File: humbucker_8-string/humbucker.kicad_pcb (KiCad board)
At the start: 2 copper layers, 102 parts, among them J1 CONN_02X04, J2 CONN_01X03, U1/2 TL072, U3/4 TL072, U5/6 TL072, U7/8 TL072

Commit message: humbucker fix
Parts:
- turned C11 to 0 degrees
- turned C31 to 0 degrees
- turned C32 to 0 degrees
- turned C51 to 0 degrees
- turned C71 to 0 degrees
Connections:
- C11 pad 1: Net-(C11-Pad1) -> GND
- C12 pad 1: +9V -> GND
- C12 pad 2: Net-(C12-Pad2) -> +9V
- C31 pad 1: Net-(C31-Pad1) -> GND
- C32 pad 2: Net-(C32-Pad2) -> GND
- C51 pad 1: Net-(C51-Pad1) -> GND
- C52 pad 1: +9V -> GND
- C52 pad 2: Net-(C52-Pad2) -> +9V
- C71 pad 1: Net-(C71-Pad1) -> GND
- C72 pad 1: +9V -> GND
- C72 pad 2: Net-(C72-Pad2) -> +9V
- U1/2 pad 4: Net-(C11-Pad1) -> -9VA
- U1/2 pad 8: Net-(C12-Pad2) -> +9V
- U3/4 pad 4: Net-(C31-Pad1) -> -9VA
- U3/4 pad 8: Net-(C32-Pad2) -> +9V
- U5/6 pad 4: Net-(C51-Pad1) -> -9VA
- U5/6 pad 8: Net-(C52-Pad2) -> +9V
- U7/8 pad 4: Net-(C71-Pad1) -> -9VA
- U7/8 pad 8: Net-(C72-Pad2) -> +9V
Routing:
- net GND: track 309.6 -> 363.5 mm, vias 0 -> 8
- net -9VA: track 130.8 -> 153.2 mm
- net +9V: track 102.6 -> 122.1 mm
- net Net-(C72-Pad2): track 2.55 -> 0.00 mm
- net Net-(C52-Pad2): track 2.55 -> 0.00 mm
- net Net-(C51-Pad1): track 2.55 -> 0.00 mm
- net Net-(C31-Pad1): track 2.55 -> 0.00 mm
- net Net-(C12-Pad2): track 2.55 -> 0.00 mm
- net Net-(C11-Pad1): track 2.55 -> 0.00 mm
- net Net-(C71-Pad1): track 2.44 -> 0.00 mm
- net Net-(C32-Pad2): track 2.44 -> 0.00 mm

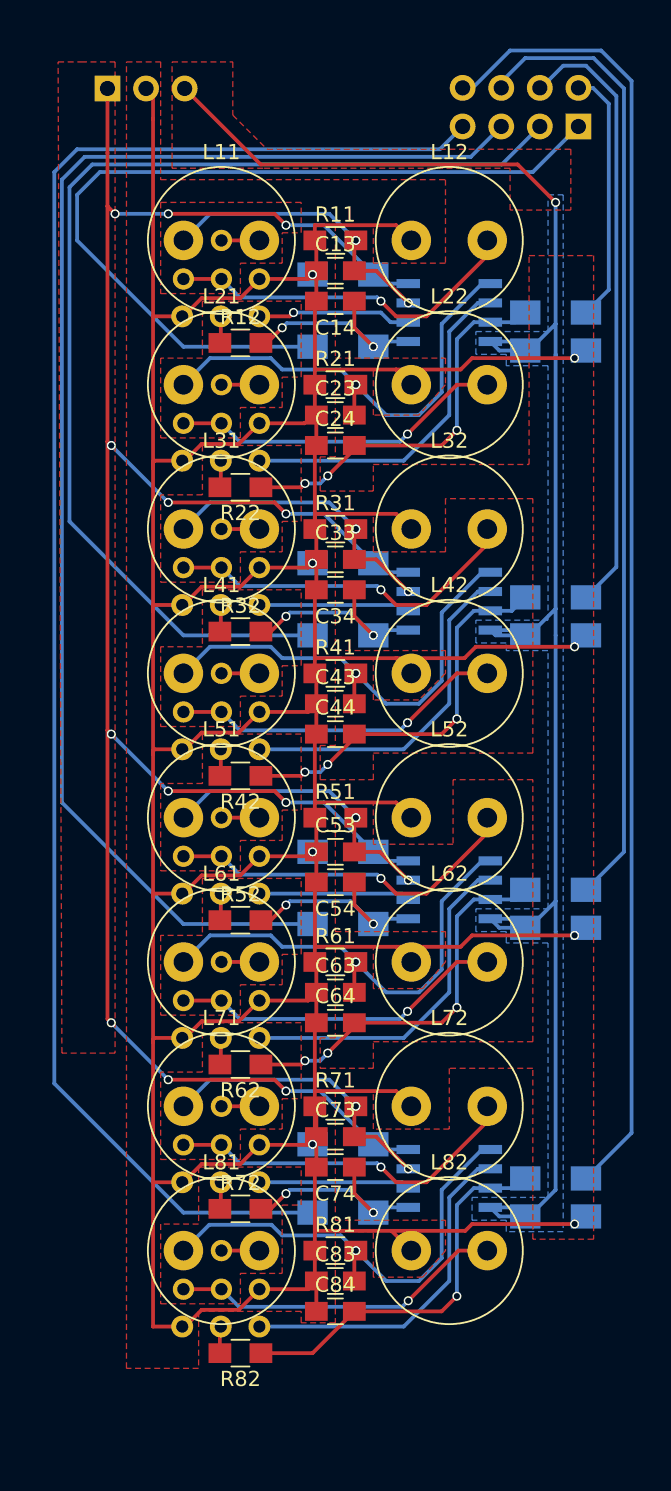
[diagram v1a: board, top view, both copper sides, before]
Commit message: humbucker: add mounting holes & dimensions
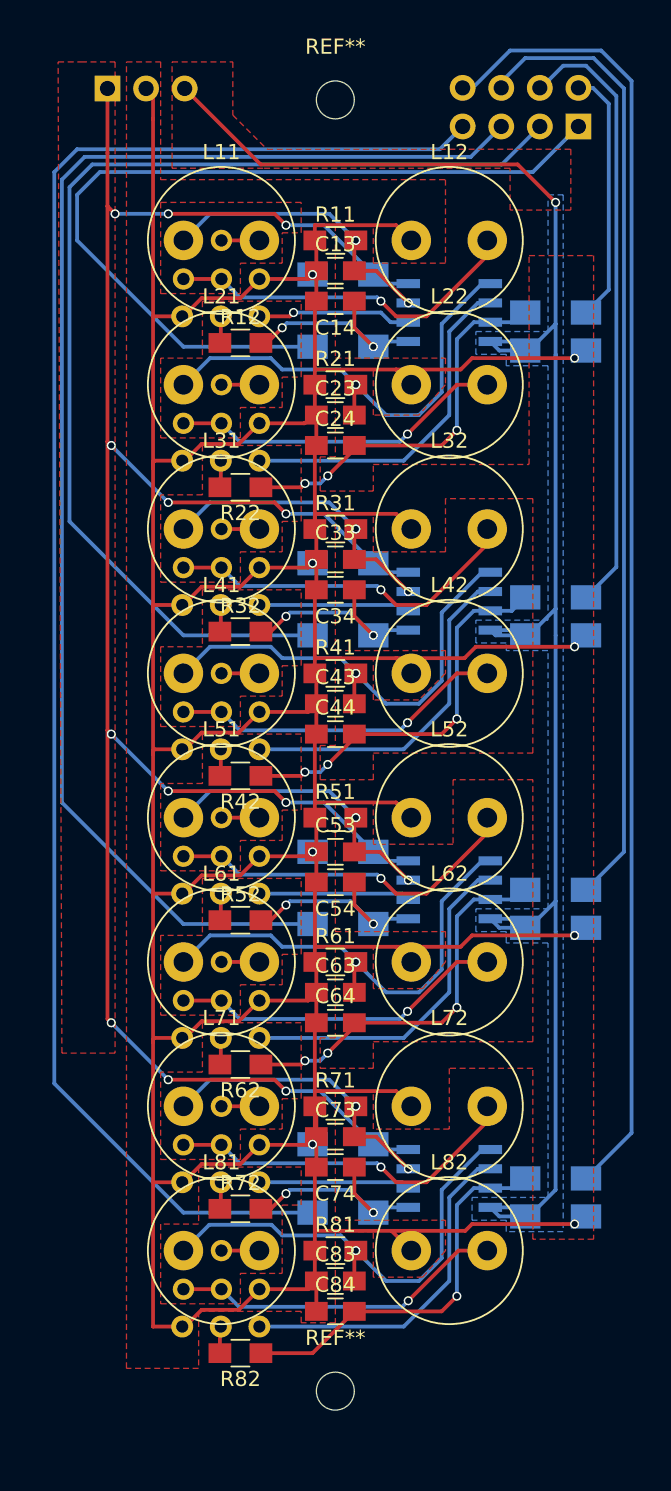
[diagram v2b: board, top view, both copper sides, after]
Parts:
- added REF**: MountingHole_2.5mm, Mounting_Holes:MountingHole_2.5mm, F.Cu at (154.0, 67.8)
- added REF**: MountingHole_2.5mm, Mounting_Holes:MountingHole_2.5mm, F.Cu at (154.0, 152.8)
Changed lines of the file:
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@@
     (links 184)
     (no_connects 0)
-    (area 0 0 0 0)
+    (area 134 61.966666 181.85 157.950001)
     (thickness 1.6)
-    (drawings 0)
+    (drawings 1)
     (tracks 622)
     (zones 0)
-    (modules 102)
+    (modules 104)
     (nets 60)
   )
@@
     (pad_to_mask_clearance 0.2)
     (aux_axis_origin 0 0)
+    (grid_origin 154 110.25)
     (visible_elements FFFCFF9F)
     (pcbplotparams
@@
       (net 59 "Net-(JP82-Pad2)"))
   )
+  (module Mounting_Holes:MountingHole_2.5mm (layer F.Cu)
+    (at 154 67.75)
+    (descr "Mounting Hole 2.5mm, no annular")
+    (tags "mounting hole 2.5mm no annular")
+    (fp_text reference REF** (at 0 -3.5) (layer F.SilkS)
+      (effects (font (size 1 1) (thickness 0.15)))
+    )
+    (fp_text value MountingHole_2.5mm (at 0 3.5) (layer F.Fab)
+      (effects (font (size 1 1) (thickness 0.15)))
+    )
+    (fp_circle (center 0 0) (end 2.5 0) (layer Cmts.User) (width 0.15))
+    (fp_circle (center 0 0) (end 2.75 0) (layer F.CrtYd) (width 0.05))
+    (pad 1 np_thru_hole circle (at 0 0) (size 2.5 2.5) (drill 2.5) (layers *.Cu *.Mask))
+  )
+  (module Mounting_Holes:MountingHole_2.5mm (layer F.Cu)
+    (at 154 152.75)
+    (descr "Mounting Hole 2.5mm, no annular")
+    (tags "mounting hole 2.5mm no annular")
+    (fp_text reference REF** (at 0 -3.5) (layer F.SilkS)
+      (effects (font (size 1 1) (thickness 0.15)))
+    )
+    (fp_text value MountingHole_2.5mm (at 0 3.5) (layer F.Fab)
+      (effects (font (size 1 1) (thickness 0.15)))
+    )
+    (fp_circle (center 0 0) (end 2.5 0) (layer Cmts.User) (width 0.15))
+    (fp_circle (center 0 0) (end 2.75 0) (layer F.CrtYd) (width 0.05))
+    (pad 1 np_thru_hole circle (at 0 0) (size 2.5 2.5) (drill 2.5) (layers *.Cu *.Mask))
+  )
+  (dimension 40 (width 0.3) (layer Margin)
+    (gr_text "40,000 mm" (at 154 156.6) (layer Margin)
+      (effects (font (size 1.5 1.5) (thickness 0.3)))
+    )
+    (feature1 (pts (xy 174 62.75) (xy 174 157.95)))
+    (feature2 (pts (xy 134 62.75) (xy 134 157.95)))
+    (crossbar (pts (xy 134 155.25) (xy 174 155.25)))
+    (arrow1a (pts (xy 174 155.25) (xy 172.873496 155.836421)))
+    (arrow1b (pts (xy 174 155.25) (xy 172.873496 154.663579)))
+    (arrow2a (pts (xy 134 155.25) (xy 135.126504 155.836421)))
+    (arrow2b (pts (xy 134 155.25) (xy 135.126504 154.663579)))
+  )
   (segment (start 150.75 76) (end 153.25 76) (width 0.25) (layer B.Cu) (net 1))

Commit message: add edge cuts
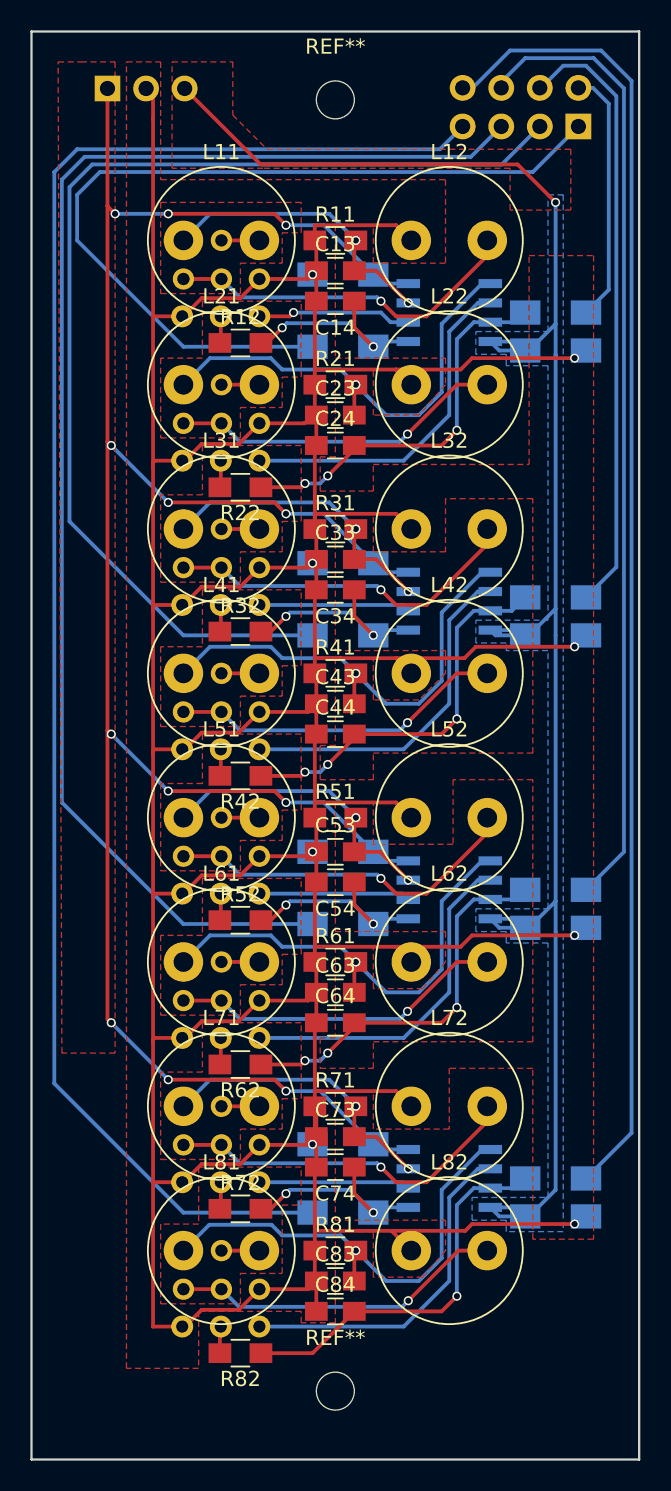
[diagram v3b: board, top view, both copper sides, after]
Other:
- board outline added: 40 x 94 mm
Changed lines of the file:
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@@
     (links 184)
     (no_connects 0)
-    (area 134 61.966666 181.85 157.950001)
+    (area 133.924999 63.174999 174.075001 157.325001)
     (thickness 1.6)
-    (drawings 1)
+    (drawings 4)
     (tracks 622)
     (zones 0)
@@
     (pad 1 np_thru_hole circle (at 0 0) (size 2.5 2.5) (drill 2.5) (layers *.Cu *.Mask))
   )
-  (dimension 40 (width 0.3) (layer Margin)
-    (gr_text "40,000 mm" (at 154 156.6) (layer Margin)
-      (effects (font (size 1.5 1.5) (thickness 0.3)))
-    )
-    (feature1 (pts (xy 174 62.75) (xy 174 157.95)))
-    (feature2 (pts (xy 134 62.75) (xy 134 157.95)))
-    (crossbar (pts (xy 134 155.25) (xy 174 155.25)))
-    (arrow1a (pts (xy 174 155.25) (xy 172.873496 155.836421)))
-    (arrow1b (pts (xy 174 155.25) (xy 172.873496 154.663579)))
-    (arrow2a (pts (xy 134 155.25) (xy 135.126504 155.836421)))
-    (arrow2b (pts (xy 134 155.25) (xy 135.126504 154.663579)))
-  )
+  (gr_line (start 174 157.25) (end 174 63.25) (angle 90) (layer Edge.Cuts) (width 0.15))
+  (gr_line (start 134 63.25) (end 134 157.25) (angle 90) (layer Edge.Cuts) (width 0.15))
+  (gr_line (start 134 157.25) (end 174 157.25) (angle 90) (layer Edge.Cuts) (width 0.15))
+  (gr_line (start 134 63.25) (end 174 63.25) (angle 90) (layer Edge.Cuts) (width 0.15))
   (segment (start 150.75 76) (end 153.25 76) (width 0.25) (layer B.Cu) (net 1))
   (via (at 139.5 75.25) (size 0.6) (drill 0.4) (layers F.Cu B.Cu) (net 1))
